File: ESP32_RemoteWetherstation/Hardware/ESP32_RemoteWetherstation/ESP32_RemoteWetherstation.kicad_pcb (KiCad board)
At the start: 2 copper layers, 27 x 45.5 mm, 43 parts, among them IC301 AP2210K-3.3TRG1, J301 BOOT, J302 UART, J303 VCC, J304 GND, J305 OpenDrain, J306 OpenDrain, J307 OpenDrain, J308 OpenDrain, J310 Analog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

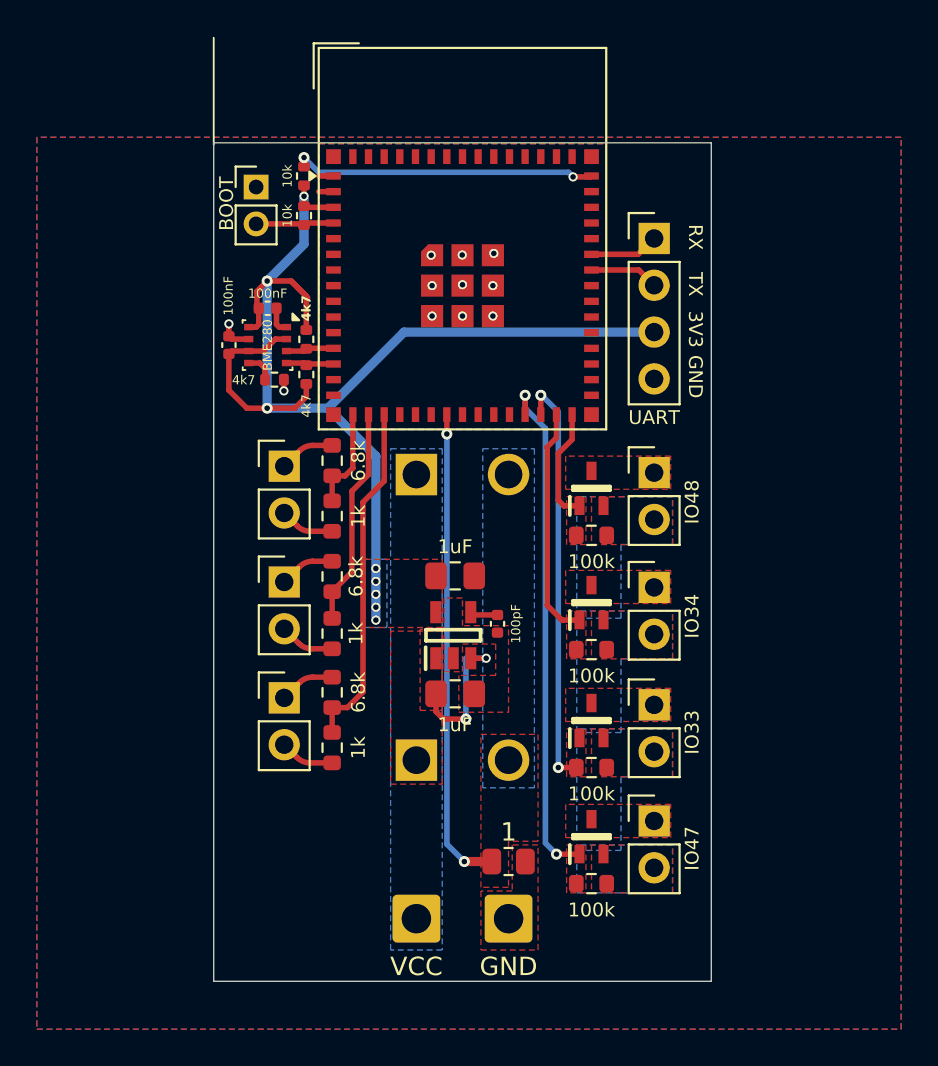
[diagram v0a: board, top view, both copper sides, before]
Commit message: chor: error correction after DRC
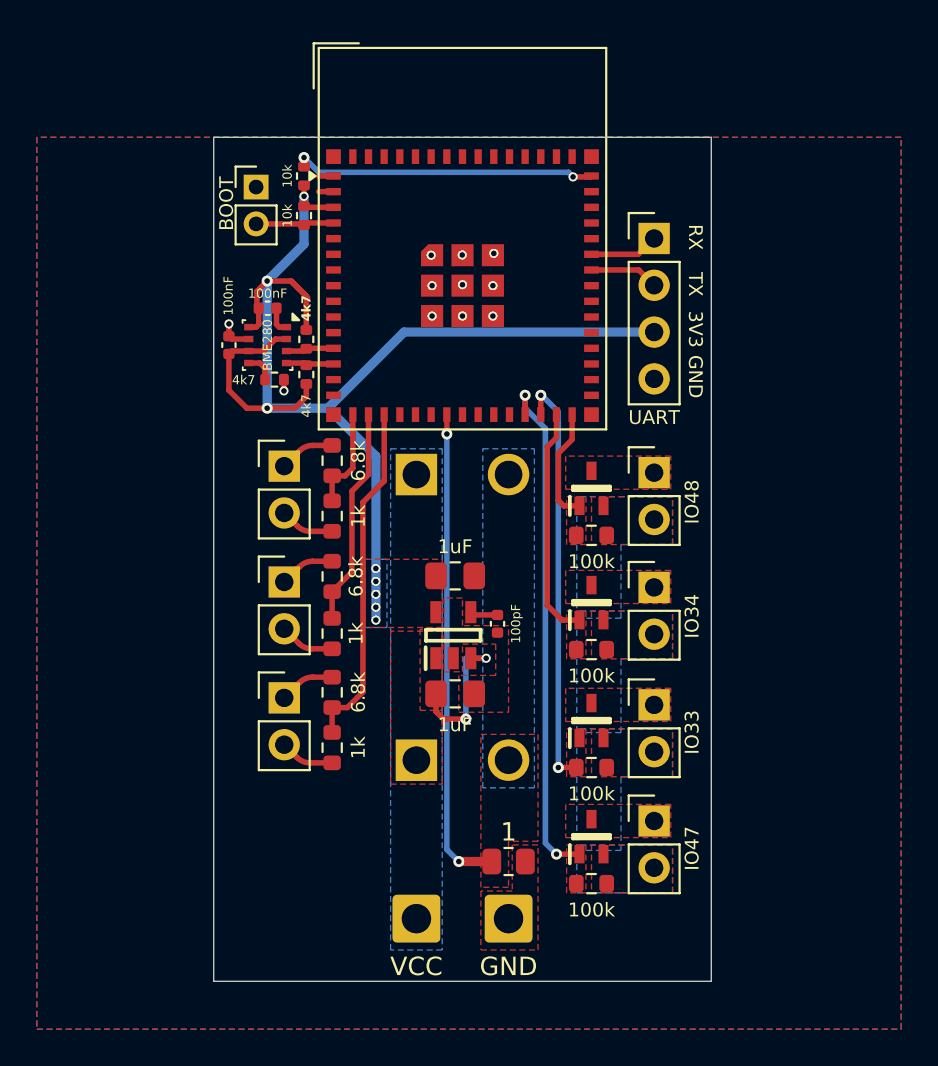
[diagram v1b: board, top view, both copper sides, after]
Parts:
- moved NT601 0.30 mm to (55.9, 138.9)
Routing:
- removed copper zone on B.Cu, net IO18
- removed copper zone on F.Cu, net IO18
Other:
- board size 27 x 45.5 mm -> 27 x 45.8 mm
- board text added: "needed: USB-connection for programming Beschriftung optionel: zone priorities"
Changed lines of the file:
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@@
 	(footprint "NetTie:NetTie-2_SMD_Pad0.5mm"
 		(layer "F.Cu")
-		(at 56.2 138.9 180)
+		(at 55.9 138.9 180)
 		(descr "Net tie, 2 pin, 0.5mm square SMD pads")
 		(tags "net tie")
@@
 		)
 	)
-	(gr_line
-		(start 42.1 94.2)
-		(end 42.1 100)
-		(stroke
-			(width 0.1)
-			(type default)
-		)
-		(layer "F.SilkS")
-	)
 	(gr_rect
-		(start 42.1 99.9)
+		(start 42.1 99.6)
 		(end 69.1 145.4)
 		(stroke
@@
 		)
 	)
-	(dimension
-		(type orthogonal)
-		(layer "F.SilkS")
-		(pts
-			(xy 63.4 99.95) (xy 69.1 99.95)
-		)
-		(height -11.85)
-		(orientation 0)
-		(format
-			(prefix "")
-			(suffix "")
-			(units 3)
-			(units_format 0)
-			(precision 4)
-			(suppress_zeroes yes)
-		)
-		(style
-			(thickness 0.1)
-			(arrow_length 1.27)
-			(text_position_mode 0)
-			(arrow_direction outward)
-			(extension_height 0.58642)
-			(extension_offset 0.5)
-			(keep_text_aligned yes)
-		)
-		(gr_text "5,7"
-			(at 66.25 87 0)
-			(layer "F.SilkS")
-			(effects
-				(font
-					(size 1 1)
-					(thickness 0.1)
-				)
-			)
-		)
-	)
-	(dimension
-		(type orthogonal)
-		(layer "F.SilkS")
-		(pts
-			(xy 42.1 94.75) (xy 47.8 94.75)
-		)
-		(height -11.85)
-		(orientation 0)
-		(format
-			(prefix "")
-			(suffix "")
-			(units 3)
-			(units_format 0)
-			(precision 4)
-			(suppress_zeroes yes)
-		)
-		(style
-			(thickness 0.1)
-			(arrow_length 1.27)
-			(text_position_mode 0)
-			(arrow_direction outward)
-			(extension_height 0.58642)
-			(extension_offset 0.5)
-			(keep_text_aligned yes)
-		)
-		(gr_text "5,7"
-			(at 44.95 81.8 0)
-			(layer "F.SilkS")
-			(effects
-				(font
-					(size 1 1)
-					(thickness 0.1)
-				)
-			)
-		)
-	)
-	(dimension
-		(type orthogonal)
-		(layer "F.SilkS")
-		(pts
-			(xy 64.62 103.71) (xy 63.4 103.71)
-		)
-		(height -8.96)
-		(orientation 0)
-		(format
-			(prefix "")
-			(suffix "")
-			(units 3)
-			(units_format 0)
-			(precision 4)
-			(suppress_zeroes yes)
-		)
-		(style
-			(thickness 0.1)
-			(arrow_length 1.27)
-			(text_position_mode 0)
-			(arrow_direction outward)
-			(extension_height 0.58642)
-			(extension_offset 0.5)
-			(keep_text_aligned yes)
-		)
-		(gr_text "1,22"
-			(at 64.01 93.65 0)
-			(layer "F.SilkS")
-			(effects
-				(font
-					(size 1 1)
-					(thickness 0.1)
-				)
+	(gr_text "needed:\nUSB-connection for programming\nBeschriftung\noptionel:\nzone priorities "
+		(at 87.4 114.5 0)
+		(layer "User.2")
+		(effects
+			(font
+				(size 1.5 1.5)
+				(thickness 0.3)
+				(bold yes)
 			)
+			(justify left bottom)
 		)
 	)
@@
 	)
 	(via
-		(at 55.7 138.9)
+		(at 55.4 138.9)
 		(size 0.6)
 		(drill 0.3)
@@
 	)
 	(segment
-		(start 54.75 115.7)
-		(end 54.75 137.95)
+		(start 55.4 138.9)
+		(end 54.75 138.25)
 		(width 0.3)
 		(layer "B.Cu")
@@
 	)
 	(segment
-		(start 54.75 137.95)
-		(end 55.7 138.9)
+		(start 54.75 138.25)
+		(end 54.75 115.7)
 		(width 0.3)
 		(layer "B.Cu")
@@
 	)
 	(segment
-		(start 56.7 138.9)
-		(end 57.1875 138.9)
-		(width 0.3)
-		(layer "F.Cu")
-		(net 54)
-	)
-	(segment
 		(start 42.925 109.725)
 		(end 42.925 110.395)
@@
 	)
 	(segment
+		(start 56.4 138.9)
+		(end 57.1875 138.9)
+		(width 0.5)
+		(layer "F.Cu")
+		(net 54)
+	)
+	(segment
 		(start 46.619426 133.252718)
 		(end 45.927319 132.560611)
@@
 	)
 	(zone
-		(net 37)
-		(net_name "IO18")
+		(net 54)
+		(net_name "GND")
 		(layer "F.Cu")
 		(hatch edge 0.5)
@@
 	)
 	(zone
-		(net 37)
-		(net_name "IO18")
+		(net 54)
+		(net_name "GND")
 		(layer "F.Cu")
 		(hatch edge 0.5)
@@
 	)
 	(zone
-		(net 37)
-		(net_name "IO18")
+		(net 54)
+		(net_name "GND")
 		(layer "F.Cu")
 		(hatch edge 0.5)
@@
 	)
 	(zone
-		(net 37)
-		(net_name "IO18")
+		(net 54)
+		(net_name "GND")
 		(layer "F.Cu")
 		(hatch edge 0.5)
@@
 	)
 	(zone
-		(net 37)
-		(net_name "IO18")
+		(net 54)
+		(net_name "GND")
 		(layer "F.Cu")
 		(hatch edge 0.5)
@@
 		(layers "F.Cu" "B.Cu")
 		(hatch edge 0.5)
-		(priority 6)
-		(connect_pads
-			(clearance 0)
-		)
-		(min_thickness 0.25)
-		(filled_areas_thickness no)
-		(fill yes
-			(thermal_gap 0.5)
-			(thermal_bridge_width 0.5)
-		)
-		(polygon
-			(pts
-				(xy 47.8 99.95) (xy 63.4 99.95) (xy 63.4 115.45) (xy 47.8 115.45)
-			)
-		)
-	)
-	(zone
-		(net 54)
-		(net_name "GND")
-		(layers "F.Cu" "B.Cu")
-		(hatch edge 0.5)
 		(connect_pads yes
 			(clearance 0)
@@
 	)
 	(zone
-		(net 37)
-		(net_name "IO18")
+		(net 54)
+		(net_name "GND")
 		(layer "B.Cu")
 		(hatch edge 0.5)
@@
 	)
 	(zone
-		(net 37)
-		(net_name "IO18")
+		(net 54)
+		(net_name "GND")
 		(layer "B.Cu")
 		(hatch edge 0.5)
@@
 	)
 	(zone
-		(net 37)
-		(net_name "IO18")
+		(net 54)
+		(net_name "GND")
 		(layer "B.Cu")
 		(hatch edge 0.5)
-		(priority 5)
+		(priority 3)
 		(connect_pads yes
 			(clearance 0)
@@
 	)
 	(zone
-		(net 37)
-		(net_name "IO18")
+		(net 54)
+		(net_name "GND")
 		(layer "B.Cu")
 		(hatch edge 0.5)
-		(priority 5)
+		(priority 1)
 		(connect_pads yes
 			(clearance 0)
@@
 	)
 	(zone
-		(net 37)
-		(net_name "IO18")
+		(net 54)
+		(net_name "GND")
 		(layer "B.Cu")
 		(hatch edge 0.5)
-		(priority 5)
+		(priority 2)
 		(connect_pads yes
 			(clearance 0)
@@
 		(members "0812cdc4-da1e-47c3-a2dd-a7f7dea9019f" "0ef5df85-36fb-41fd-b4ed-e7969aa49ba2"
 			"14175c9b-99a3-4680-b3f3-9a9bc148d6bc" "17df271f-6c42-4326-a4a6-9cc5704ad734"
-			"3b810030-adf9-49c6-ab36-72c1a7a72adb" "3f00e3fb-068a-4d87-a54c-3c5f56afa3ed"
-			"5adc4041-a35a-4f33-b9fe-145ad42367c6" "5ce9c1a6-e039-4b40-9984-29df755d5da0"
-			"6ef5f003-afd5-4a19-ae6c-b8c9535cc63f" "9418ed2d-b000-4be8-bdb1-45d061acf82f"
-			"9834adff-0b9c-48c5-87c9-3aa3899a5ed9" "9ba9ef86-2e62-4915-8b55-de18afd58ffa"
-			"b328757d-9847-4438-9930-f738eb0a7138" "b5124269-94fe-4ad2-ab52-df939cced739"
-			"cb6e27c6-9684-4fe0-a440-b3452dc7a1ac" "d20f2521-dbc0-4e0e-aca7-a2ae8faff05c"
-			"e66c877c-4f90-4a8e-b8ed-aa73f78fd67a" "eac791e9-d991-4b81-a691-516ad0226fb5"
-			"f0b9288f-cf68-4cb4-b6af-45092ccd18fe" "f0fe11fa-2994-49ff-8e03-22fc130350fb"
+			"3f00e3fb-068a-4d87-a54c-3c5f56afa3ed" "5adc4041-a35a-4f33-b9fe-145ad42367c6"
+			"5ce9c1a6-e039-4b40-9984-29df755d5da0" "6ef5f003-afd5-4a19-ae6c-b8c9535cc63f"
+			"9418ed2d-b000-4be8-bdb1-45d061acf82f" "9834adff-0b9c-48c5-87c9-3aa3899a5ed9"
+			"9ba9ef86-2e62-4915-8b55-de18afd58ffa" "b328757d-9847-4438-9930-f738eb0a7138"
+			"b5124269-94fe-4ad2-ab52-df939cced739" "cb6e27c6-9684-4fe0-a440-b3452dc7a1ac"
+			"d20f2521-dbc0-4e0e-aca7-a2ae8faff05c" "e66c877c-4f90-4a8e-b8ed-aa73f78fd67a"
+			"eac791e9-d991-4b81-a691-516ad0226fb5" "f0b9288f-cf68-4cb4-b6af-45092ccd18fe"
+			"f0fe11fa-2994-49ff-8e03-22fc130350fb"
 		)
 	)
